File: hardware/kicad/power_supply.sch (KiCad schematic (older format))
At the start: 0 parts

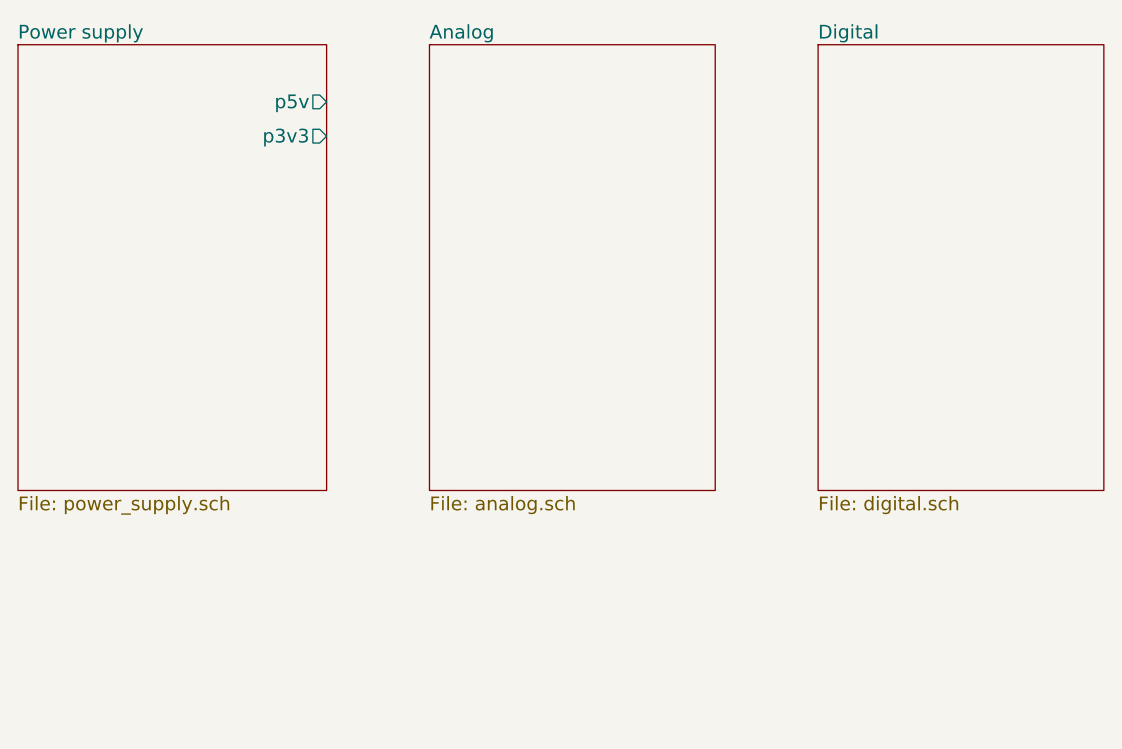
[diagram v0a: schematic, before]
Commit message: Added sheets for KiCAD.
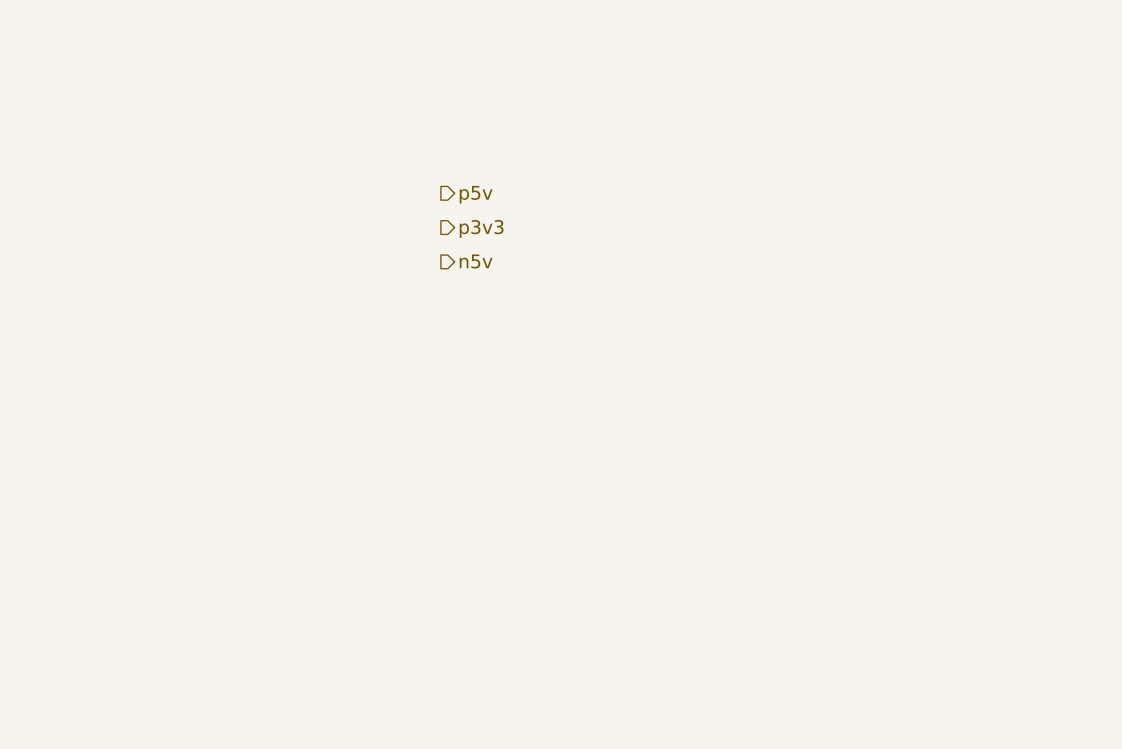
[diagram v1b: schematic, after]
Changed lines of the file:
@@
 $Descr A4 11693 8268
 encoding utf-8
-Sheet 1 4
+Sheet 2 4
 Title ""
 Date ""
@@
 Comment4 ""
 $EndDescr
-$Sheet
-S 2400 1200 1350 1950
-U 57FA5DAC
-F0 "Power supply" 60
-F1 "power_supply.sch" 60
-F2 "p5v" O R 3750 1450 60
-F3 "p3v3" O R 3750 1600 60
-$EndSheet
-$Sheet
-S 4200 1200 1250 1950
-U 57FA5DCE
-F0 "Analog" 60
-F1 "analog.sch" 60
-$EndSheet
-$Sheet
-S 5900 1200 1250 1950
-U 57FA5DF6
-F0 "Digital" 60
-F1 "digital.sch" 60
-$EndSheet
+Text HLabel 4250 1850 2    60   Output ~ 0
+p5v
+Text HLabel 4250 2000 2    60   Output ~ 0
+p3v3
+Text HLabel 4250 2150 2    60   Output ~ 0
+n5v
 $EndSCHEMATC

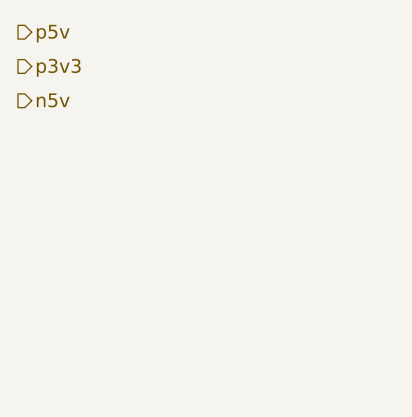
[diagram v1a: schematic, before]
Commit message: Added Modex library and hierarchial sheets for power, analog and digital circuitry.
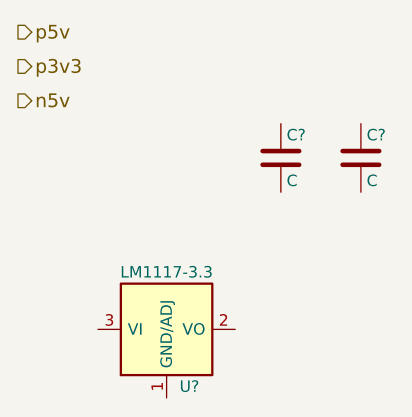
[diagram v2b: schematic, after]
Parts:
- added C? (x2): C, symbol C
- added U?: LM1117-3.3, symbol LM1117-3.3
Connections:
- new net: U?.2 (VO), U?.4 (VO)
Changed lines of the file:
@@
 LIBS:valves
 LIBS:microchip_dspic33dsc
+LIBS:modex
 LIBS:ultrasonic_anemometer-cache
 EELAYER 25 0
@@
 Text HLabel 4250 2150 2    60   Output ~ 0
 n5v
+$Comp
+L C C?
+U 1 1 57FA730B
+P 5400 2400
+F 0 "C?" H 5425 2500 50  0000 L CNN
+F 1 "C" H 5425 2300 50  0000 L CNN
+F 2 "" H 5438 2250 50  0000 C CNN
+F 3 "" H 5400 2400 50  0000 C CNN
+	1    5400 2400
+	1    0    0    -1
+$EndComp
+$Comp
+L C C?
+U 1 1 57FA73F2
+P 5750 2400
+F 0 "C?" H 5775 2500 50  0000 L CNN
+F 1 "C" H 5775 2300 50  0000 L CNN
+F 2 "" H 5788 2250 50  0000 C CNN
+F 3 "" H 5750 2400 50  0000 C CNN
+	1    5750 2400
+	1    0    0    -1
+$EndComp
+$Comp
+L LM1117-3.3 U?
+U 1 1 57FA7558
+P 4900 3150
+F 0 "U?" H 5000 2900 50  0000 C CNN
+F 1 "LM1117-3.3" H 4900 3400 50  0000 C CNN
+F 2 "" H 4900 3150 50  0000 C CNN
+F 3 "" H 4900 3150 50  0000 C CNN
+	1    4900 3150
+	1    0    0    -1
+$EndComp
 $EndSCHEMATC

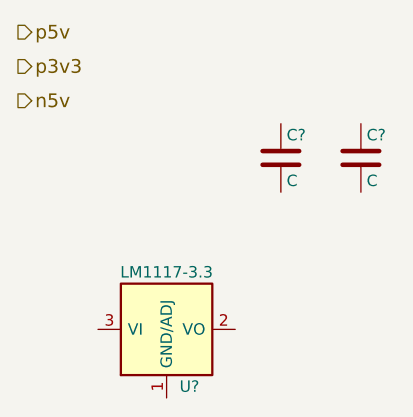
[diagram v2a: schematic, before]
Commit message: Updated schematic and PCB.
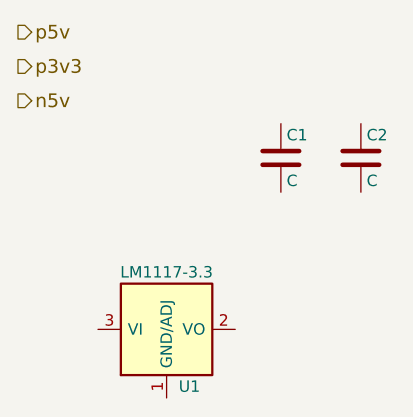
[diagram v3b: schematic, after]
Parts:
- C1, C2: renamed from C?; footprint (none) -> Capacitors_SMD:C_0805_HandSoldering
- U1: renamed from U?; footprint (none) -> TO_SOT_Packages_SMD:SOT-223
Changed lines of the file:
@@
 n5v
 $Comp
-L C C?
+L C C1
 U 1 1 57FA730B
 P 5400 2400
-F 0 "C?" H 5425 2500 50  0000 L CNN
+F 0 "C1" H 5425 2500 50  0000 L CNN
 F 1 "C" H 5425 2300 50  0000 L CNN
-F 2 "" H 5438 2250 50  0000 C CNN
+F 2 "Capacitors_SMD:C_0805_HandSoldering" H 5438 2250 50  0001 C CNN
 F 3 "" H 5400 2400 50  0000 C CNN
 	1    5400 2400
@@
 $EndComp
 $Comp
-L C C?
+L C C2
 U 1 1 57FA73F2
 P 5750 2400
-F 0 "C?" H 5775 2500 50  0000 L CNN
+F 0 "C2" H 5775 2500 50  0000 L CNN
 F 1 "C" H 5775 2300 50  0000 L CNN
-F 2 "" H 5788 2250 50  0000 C CNN
+F 2 "Capacitors_SMD:C_0805_HandSoldering" H 5788 2250 50  0001 C CNN
 F 3 "" H 5750 2400 50  0000 C CNN
 	1    5750 2400
@@
 $EndComp
 $Comp
-L LM1117-3.3 U?
+L LM1117-3.3 U1
 U 1 1 57FA7558
 P 4900 3150
-F 0 "U?" H 5000 2900 50  0000 C CNN
+F 0 "U1" H 5000 2900 50  0000 C CNN
 F 1 "LM1117-3.3" H 4900 3400 50  0000 C CNN
-F 2 "" H 4900 3150 50  0000 C CNN
+F 2 "TO_SOT_Packages_SMD:SOT-223" H 4900 3150 50  0001 C CNN
 F 3 "" H 4900 3150 50  0000 C CNN
 	1    4900 3150

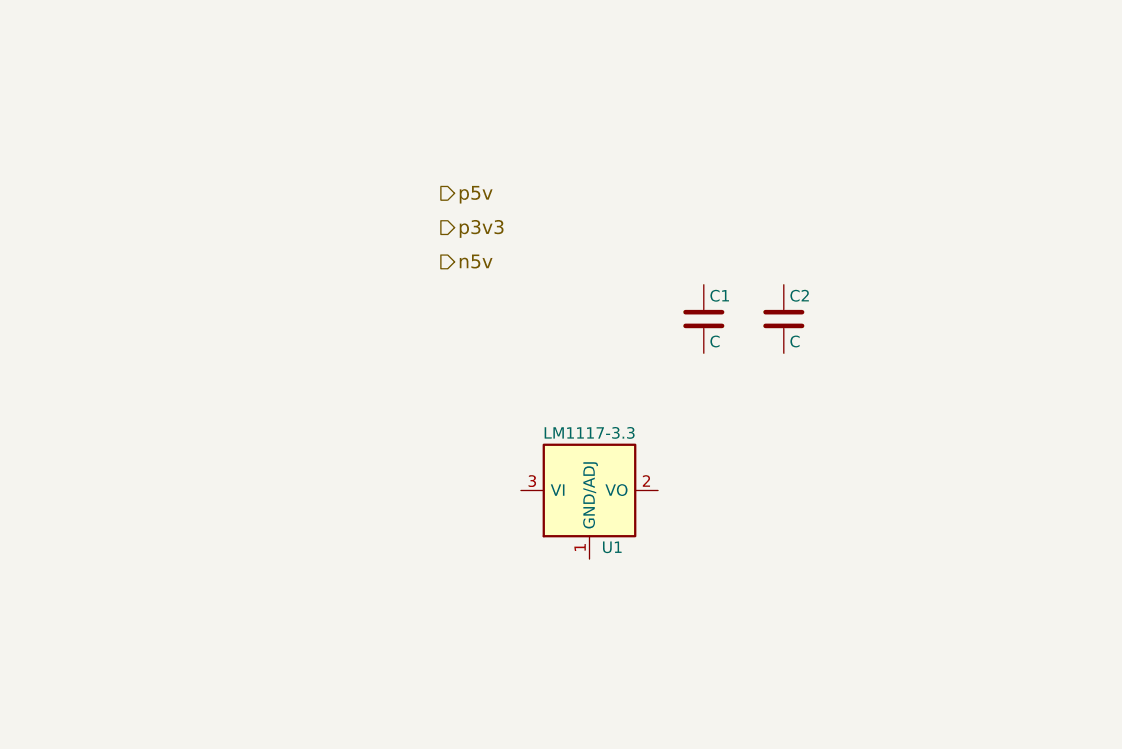
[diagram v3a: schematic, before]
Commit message: Updated schematic and PCB. Added OPAMP to the Modex library.
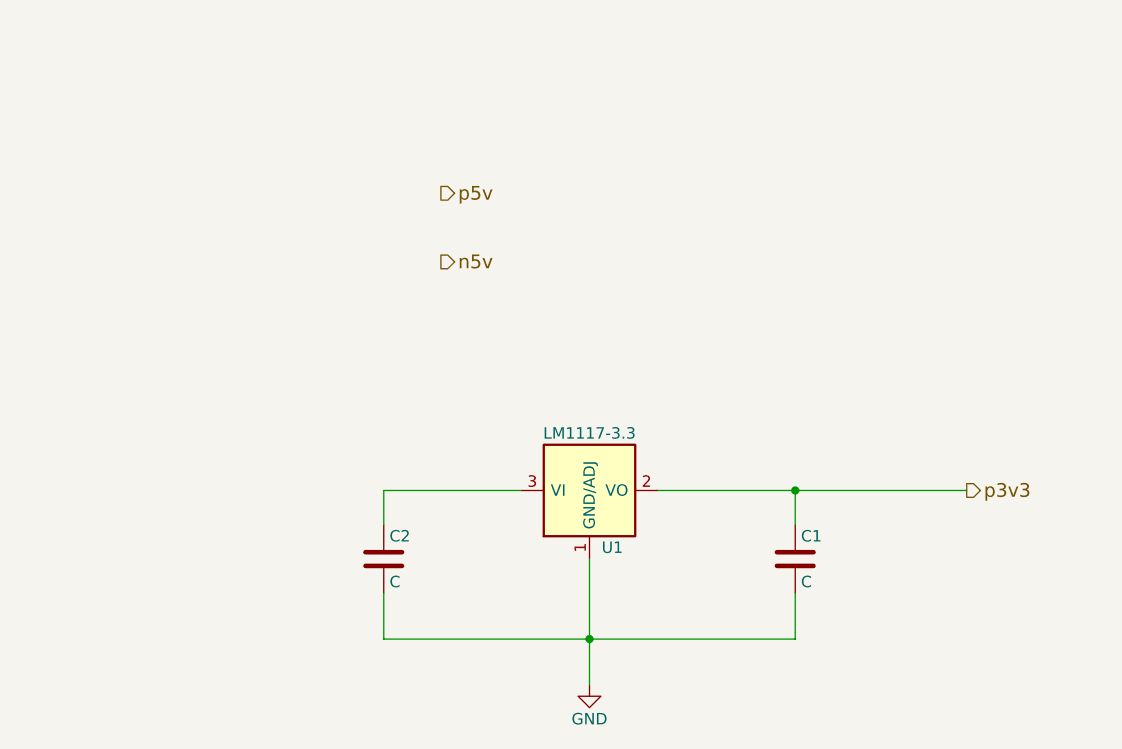
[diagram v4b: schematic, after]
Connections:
- net p3v3: now also C1.1, U1.2 (VO), U1.4 (VO)
- net GND: now reaches C1.2
- net GND: now also C2.2, U1.1 (GND/ADJ)
- net at C2.1: now also U1.3 (VI)
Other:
- moved on the sheet: C1, C2
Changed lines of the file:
@@
 Text HLabel 4250 1850 2    60   Output ~ 0
 p5v
-Text HLabel 4250 2000 2    60   Output ~ 0
+Text HLabel 6550 3150 2    60   Output ~ 0
 p3v3
 Text HLabel 4250 2150 2    60   Output ~ 0
@@
 L C C1
 U 1 1 57FA730B
-P 5400 2400
-F 0 "C1" H 5425 2500 50  0000 L CNN
-F 1 "C" H 5425 2300 50  0000 L CNN
-F 2 "Capacitors_SMD:C_0805_HandSoldering" H 5438 2250 50  0001 C CNN
-F 3 "" H 5400 2400 50  0000 C CNN
-	1    5400 2400
+P 5800 3450
+F 0 "C1" H 5825 3550 50  0000 L CNN
+F 1 "C" H 5825 3350 50  0000 L CNN
+F 2 "Capacitors_SMD:C_0805_HandSoldering" H 5838 3300 50  0001 C CNN
+F 3 "" H 5800 3450 50  0000 C CNN
+	1    5800 3450
 	1    0    0    -1
 $EndComp
@@
 L C C2
 U 1 1 57FA73F2
-P 5750 2400
-F 0 "C2" H 5775 2500 50  0000 L CNN
-F 1 "C" H 5775 2300 50  0000 L CNN
-F 2 "Capacitors_SMD:C_0805_HandSoldering" H 5788 2250 50  0001 C CNN
-F 3 "" H 5750 2400 50  0000 C CNN
-	1    5750 2400
+P 4000 3450
+F 0 "C2" H 4025 3550 50  0000 L CNN
+F 1 "C" H 4025 3350 50  0000 L CNN
+F 2 "Capacitors_SMD:C_0805_HandSoldering" H 4038 3300 50  0001 C CNN
+F 3 "" H 4000 3450 50  0000 C CNN
+	1    4000 3450
 	1    0    0    -1
 $EndComp
@@
 	1    0    0    -1
 $EndComp
+Wire Wire Line
+	4000 3300 4000 3150
+Wire Wire Line
+	4000 3150 4600 3150
+Wire Wire Line
+	5200 3150 6550 3150
+Wire Wire Line
+	5800 3300 5800 3150
+Connection ~ 5800 3150
+Wire Wire Line
+	5800 3600 5800 3800
+Wire Wire Line
+	5800 3800 4000 3800
+Wire Wire Line
+	4000 3800 4000 3600
+Wire Wire Line
+	4900 3450 4900 4000
+Connection ~ 4900 3800
+$Comp
+L GND #PWR1
+U 1 1 584C4220
+P 4900 4000
+F 0 "#PWR1" H 4900 3750 50  0001 C CNN
+F 1 "GND" H 4900 3850 50  0000 C CNN
+F 2 "" H 4900 4000 50  0000 C CNN
+F 3 "" H 4900 4000 50  0000 C CNN
+	1    4900 4000
+	1    0    0    -1
+$EndComp
